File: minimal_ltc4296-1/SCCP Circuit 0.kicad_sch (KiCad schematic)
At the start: 3 parts

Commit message: Update KiCad PCB file
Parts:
- added C13: 2.2 µF, capacitor_footprints:C_0805_2012Metric, symbol CAPACITORS_CGA4J1X7R2A_DATA_BASE:C_CGA4J1X7R2A225K125AC
- added C18: 2.2 nF, capacitor_footprints:C_0402_1005Metric, symbol CAPACITORS_C1005X7S2A_DATA_BASE:C_C1005X7S2A222K050BB
- added Q7: 100 V, transistor_footprints:SOT-323, symbol TRANSISTORS_BSS123WQ-7-F_DATA_BASE:Q_BSS123WQ-7-F
- added R27: 4.99 kΩ, resistor_footprints:R_0402_1005Metric, symbol RESISTORS_ERJ-2RKF_DATA_BASE:R_ERJ-2RKF4991X
- added R32: 10 kΩ, resistor_footprints:R_0402_1005Metric, symbol RESISTORS_ERJ-2RKF_DATA_BASE:R_ERJ-2RKF1002X
- added R37: 5.1 Ω, resistor_footprints:R_1206_3216Metric, symbol RESISTORS_RT1206FRE07_DATA_BASE:R_RT1206FRE075R1L
- added R42: 20 Ω, resistor_footprints:R_1206_3216Metric, symbol RESISTORS_RT1206FRE07_DATA_BASE:R_RT1206FRE0720RL
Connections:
- net OUTM: now also R37.2
- net OUTP: now also C13.1
- net SW: now also R27.2, R32.1
- new net: C18.1, Q7.1 (G), R32.2
- new net: C18.2, Q7.3 (D), R42.2
- new net: C13.2, R42.1
- new net: Q7.2 (S), R37.1
- new net 3V3: R27.1
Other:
- moved on the sheet: C8, D3, R22

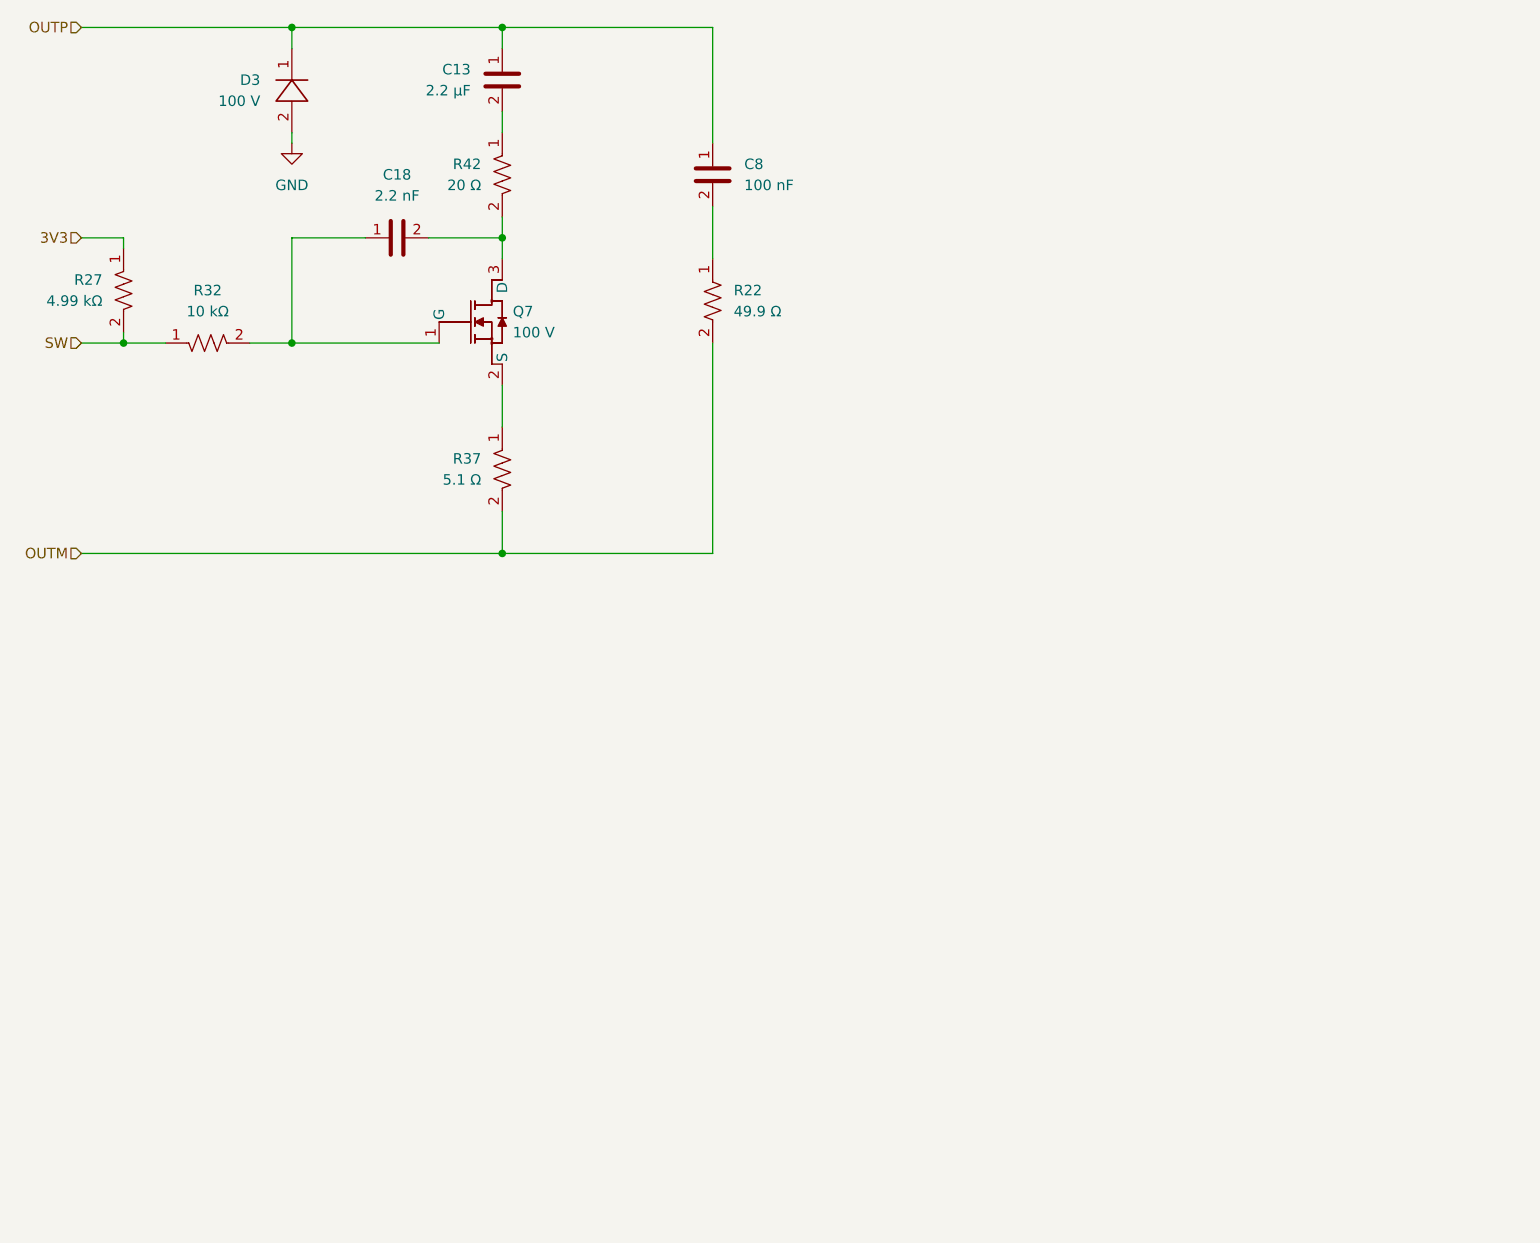
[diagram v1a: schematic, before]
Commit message: Update KiCad schematic, PCB, and symbol libraries with SCCP circuit changes
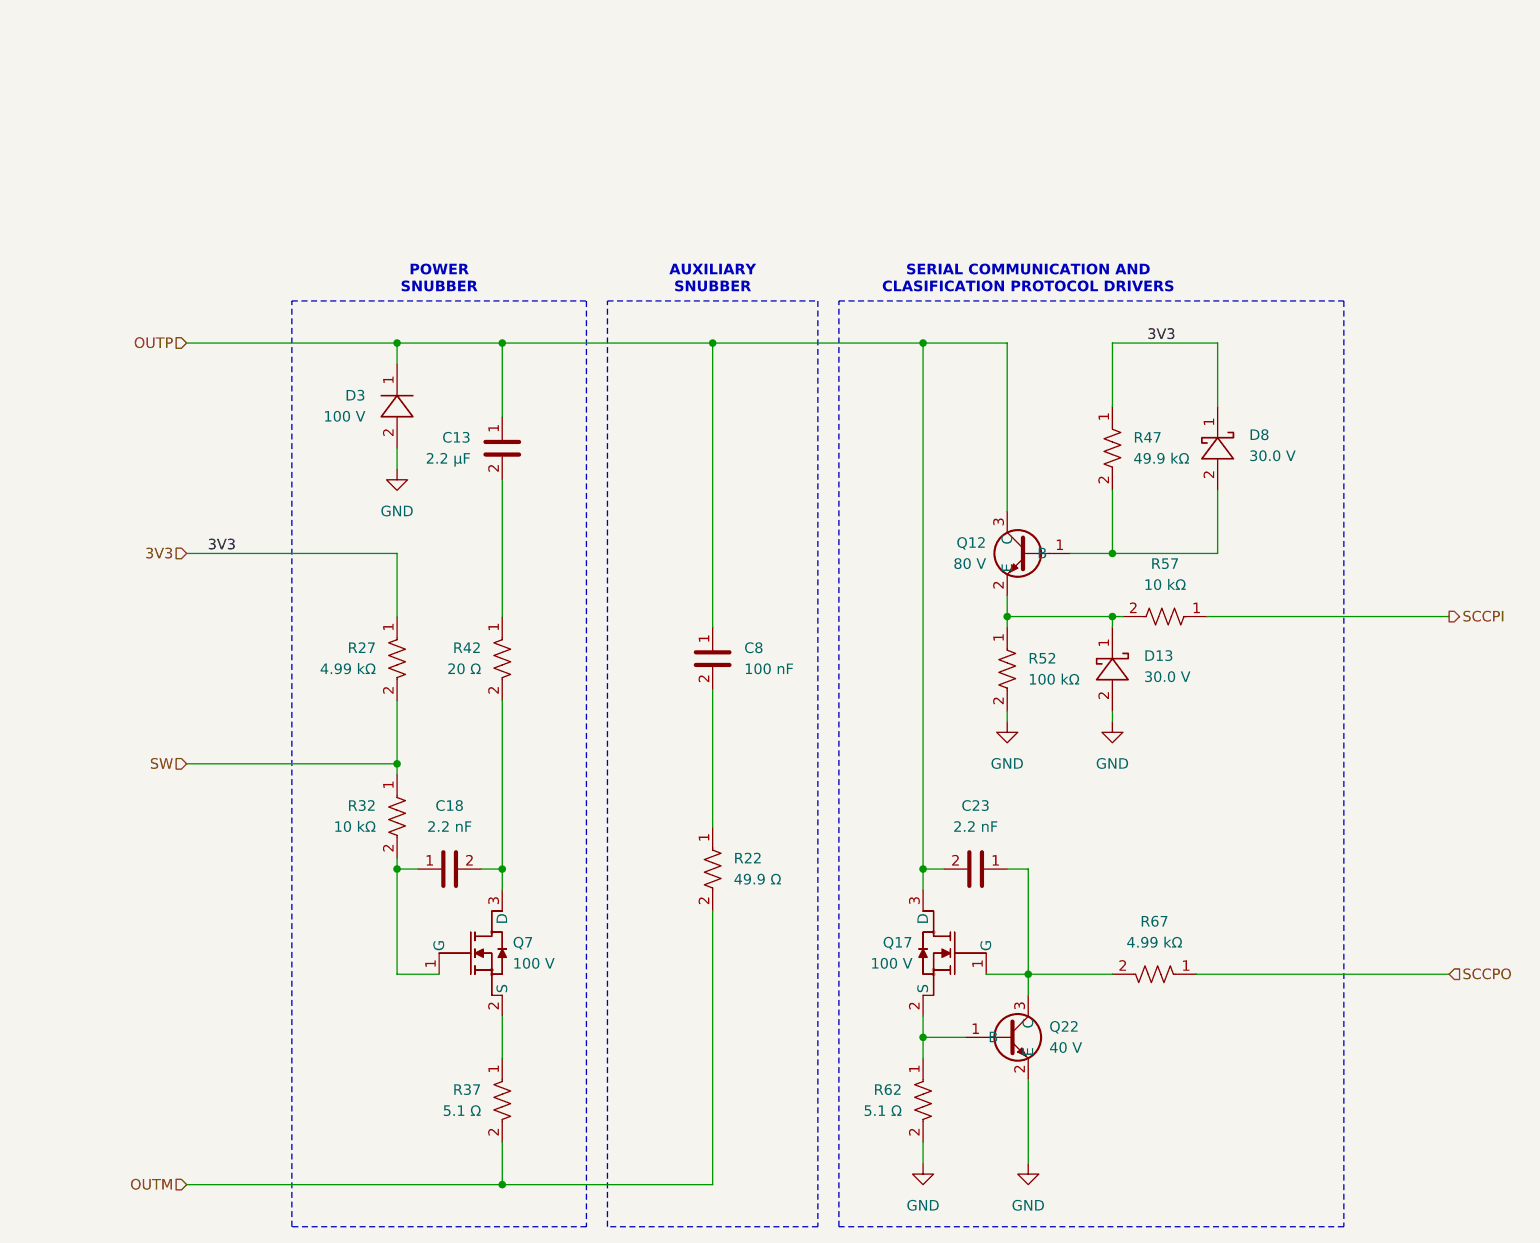
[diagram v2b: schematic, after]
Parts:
- added C23: 2.2 nF, capacitor_footprints:C_0402_1005Metric, symbol CAPACITORS_C1005X7S2A_DATA_BASE:C_C1005X7S2A222K050BB
- added D13, D8: 30.0 V, diode_footprints:SOD323F, symbol DIODES_BAT54WS-7-F_DATA_BASE:D_BAT54WS-7-F
- added Q12: 80 V, transistor_footprints:SOT23-3, symbol TRANSISTORS_MMBTA06-7-F_DATA_BASE:Q_MMBTA06-7-F
- added Q17: 100 V, transistor_footprints:SOT-323, symbol TRANSISTORS_BSS123WQ-7-F_DATA_BASE:Q_BSS123WQ-7-F
- added Q22: 40 V, transistor_footprints:SOT23-3, symbol TRANSISTORS_MMBT3904LT3G_DATA_BASE:Q_MMBT3904LT3G
- added R47: 49.9 kΩ, resistor_footprints:R_0402_1005Metric, symbol RESISTORS_ERJ-2RKF_DATA_BASE:R_ERJ-2RKF4992X
- added R52: 100 kΩ, resistor_footprints:R_0402_1005Metric, symbol RESISTORS_ERJ-2RKF_DATA_BASE:R_ERJ-2RKF1003X
- added R57: 10 kΩ, resistor_footprints:R_0402_1005Metric, symbol RESISTORS_ERJ-2RKF_DATA_BASE:R_ERJ-2RKF1002X
- added R62: 5.1 Ω, resistor_footprints:R_1206_3216Metric, symbol RESISTORS_RT1206FRE07_DATA_BASE:R_RT1206FRE075R1L
- added R67: 4.99 kΩ, resistor_footprints:R_0402_1005Metric, symbol RESISTORS_ERJ-2RKF_DATA_BASE:R_ERJ-2RKF4991X
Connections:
- net 3V3: now also D8.1, R47.1
- net GND: now also D13.2, Q22.2 (E), R52.2, R62.2
- net OUTP: now also C23.2, Q12.3 (C), Q17.3 (D)
- new net: D13.1, Q12.2 (E), R52.1, R57.2
- new net: D8.2, Q12.1 (B), R47.2
- new net: C23.1, Q17.1 (G), Q22.3 (C), R67.2
- new net: Q17.2 (S), Q22.1 (B), R62.1
- new net SCCPI: R57.1
- new net SCCPO: R67.1
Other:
- note added: "AUXILIARY SNUBBER"
- note added: "POWER SNUBBER"
- note added: "SERIAL COMMUNICATION AND CLASIFICATION PROTOCOL DRIVERS"
- moved on the sheet: C13, C18, C8, D3, Q7, R22, R27, R32, R37, R42
